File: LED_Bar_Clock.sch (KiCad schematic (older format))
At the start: 51 parts, among them J1 U262-16XN-4BVC11, J2 AVR-ISP-6, SW1 SKHMQKE010, SW2 SW_5_Way, U1 ATtiny84A-SSUR, U2 DS1307Z+, Y1 32.768 kHz

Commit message: Finish pcb routing
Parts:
- removed C2: 104, Capacitor_SMD:C_0603_1608Metric_Pad1.05x0.95mm_HandSolder, symbol Device:C_Small
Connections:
- net D+: now reaches R2.2, U1.2 (XTAL1/PB0)
- net D-: now reaches R3.2, U1.3 (XTAL2/PB1)
- net at U2.1 (X1): now also Y1.1; no longer Y1.2
- net at U2.2 (X2): now also Y1.2; no longer Y1.1
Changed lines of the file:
@@
 NoConn ~ 1700 6450
-$Comp
-L power:+5V #PWR0155
-U 1 1 5CA24AC6
-P 2300 5550
-F 0 "#PWR0155" H 2300 5400 50  0001 C CNN
-F 1 "+5V" H 2315 5723 50  0000 C CNN
-F 2 "" H 2300 5550 50  0001 C CNN
-F 3 "" H 2300 5550 50  0001 C CNN
-	1    2300 5550
-	-1   0    0    -1
-$EndComp
 $Comp
 L power:GND #PWR0157
@@
 U 1 1 5C8C5C64
 P 3150 6750
-F 0 "Y1" V 3196 6619 50  0000 R CNN
-F 1 "32.768 kHz" V 3105 6619 50  0000 R CNN
+F 0 "Y1" V 3104 6881 50  0000 L CNN
+F 1 "32.768 kHz" V 3195 6881 50  0000 L CNN
 F 2 "Crystal:Crystal_DS26_D2.0mm_L6.0mm_Horizontal" H 3150 6750 50  0001 C CNN
 F 3 "~" H 3150 6750 50  0001 C CNN
 	1    3150 6750
-	0    -1   -1   0
+	0    1    1    0
 $EndComp
 Wire Wire Line
@@
 $EndComp
 $Comp
-L Device:C_Small C2
-U 1 1 5CA3337C
-P 2450 5800
-F 0 "C2" H 2542 5846 50  0000 L CNN
-F 1 "104" H 2542 5755 50  0000 L CNN
-F 2 "Capacitor_SMD:C_0603_1608Metric_Pad1.05x0.95mm_HandSolder" H 2450 5800 50  0001 C CNN
-F 3 "~" H 2450 5800 50  0001 C CNN
-	1    2450 5800
-	1    0    0    -1
-$EndComp
-Wire Wire Line
-	2300 5550 2300 5650
-Wire Wire Line
-	2300 5650 2450 5650
-Wire Wire Line
-	2450 5650 2450 5700
-Connection ~ 2300 5650
-$Comp
-L power:GND #PWR0122
-U 1 1 5CA48238
-P 2450 5900
-F 0 "#PWR0122" H 2450 5650 50  0001 C CNN
-F 1 "GND" H 2455 5727 50  0000 C CNN
-F 2 "" H 2450 5900 50  0001 C CNN
-F 3 "" H 2450 5900 50  0001 C CNN
-	1    2450 5900
-	1    0    0    -1
-$EndComp
-Wire Wire Line
-	2300 5650 2300 6050
-$Comp
 L power:+5V #PWR0123
 U 1 1 5CA72611
@@
 	0    1    1    0
 $EndComp
+Text Label 2700 4250 0    50   ~ 0
+D+
+Text Label 2700 4350 0    50   ~ 0
+D-
+$Comp
+L power:+5V #PWR0155
+U 1 1 5CA24AC6
+P 2300 6050
+F 0 "#PWR0155" H 2300 5900 50  0001 C CNN
+F 1 "+5V" H 2315 6223 50  0000 C CNN
+F 2 "" H 2300 6050 50  0001 C CNN
+F 3 "" H 2300 6050 50  0001 C CNN
+	1    2300 6050
+	-1   0    0    -1
+$EndComp
 $EndSCHEMATC

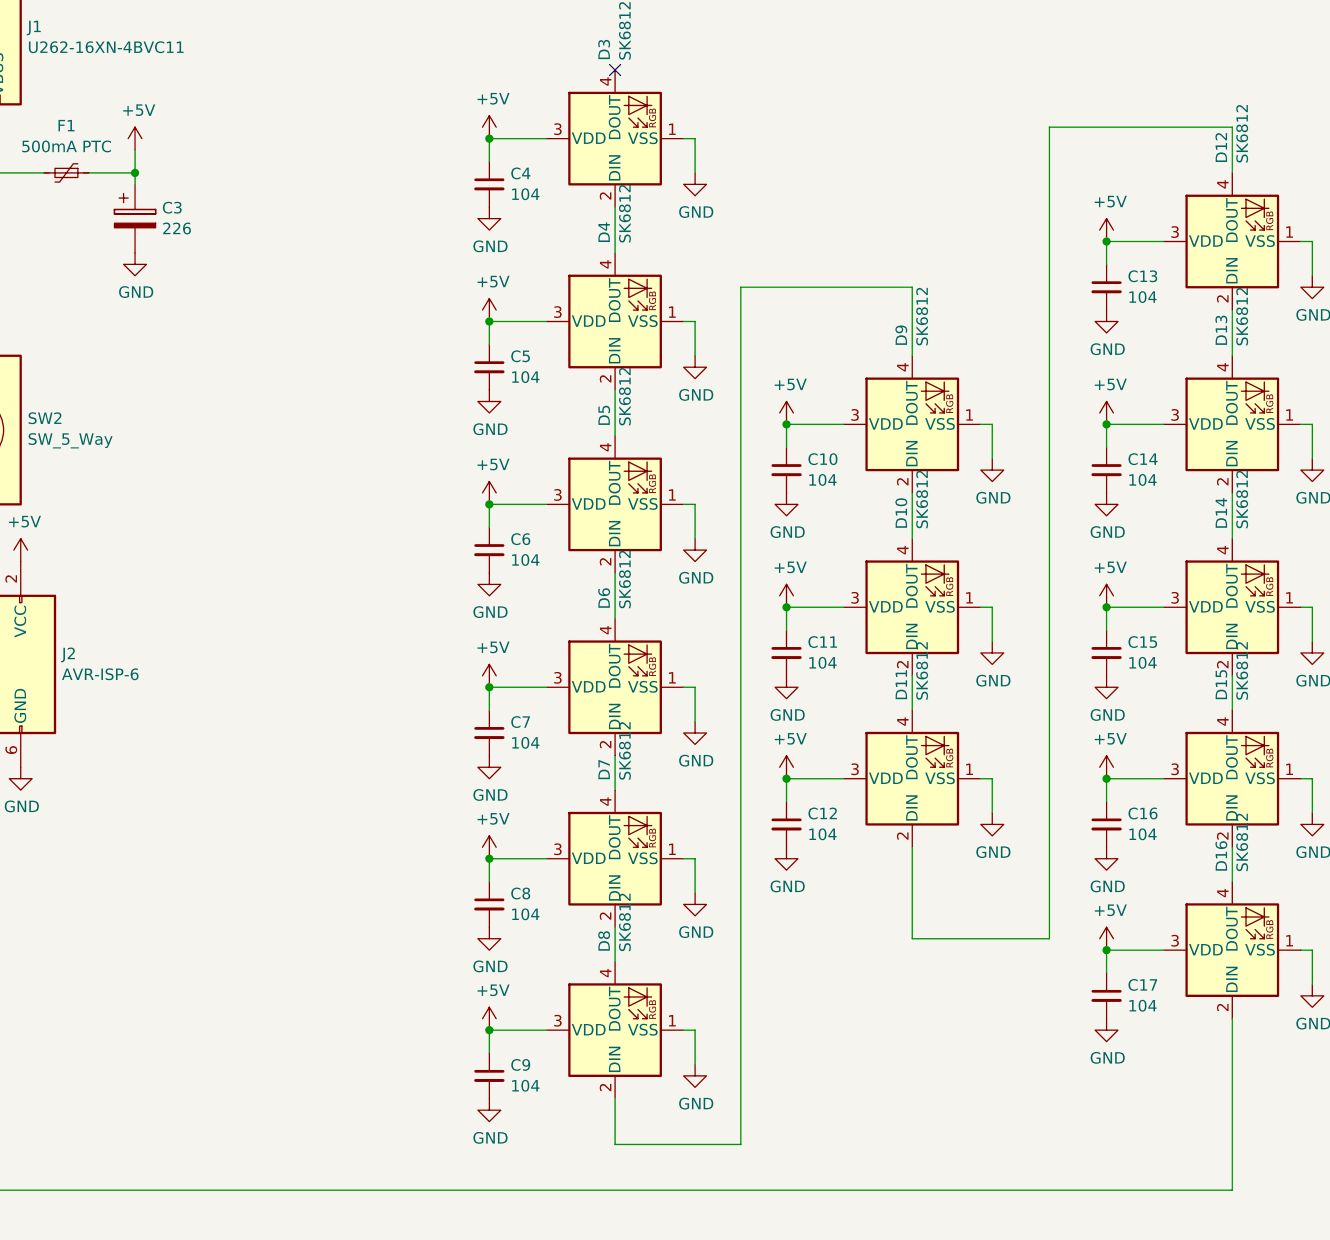
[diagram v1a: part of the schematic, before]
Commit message: fix annotations and silkscreen locations
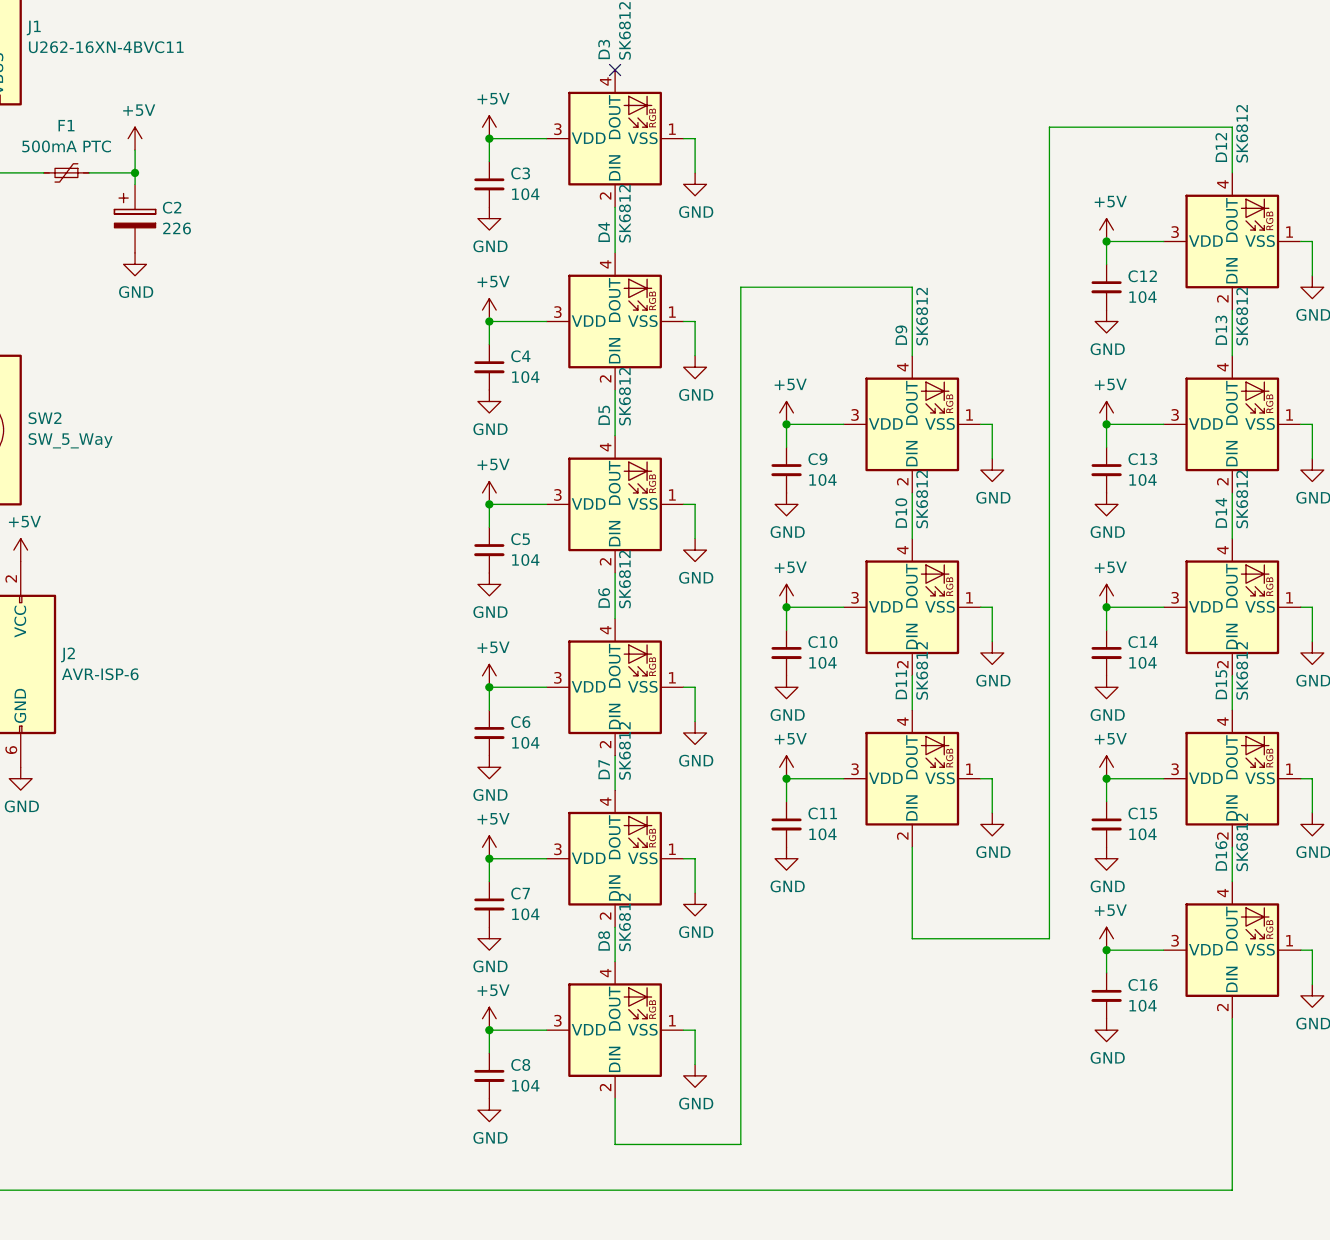
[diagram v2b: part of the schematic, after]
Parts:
- renumbered C11 to C10, C12 to C11, C13 to C12, C14 to C13, C15 to C14, C16 to C15, C17 to C16, C3 to C2, C4 to C3, C5 to C4, C6 to C5, C7 to C6, C8 to C7, C9 to C8, C10 to C9

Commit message: silkscreen and stealth labels
add a stealth footprint for the leds because we dont need silkscreen
on the front

official name is FILO Clock
first illuminated last out
.. or ..
first ignited last out
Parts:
- D10, D11, D12, D13, D14, D15, D16, D3, D4, D5, D6, D7, D8, D9: footprint LED_SMD:LED_SK6812_PLCC4_5.0x5.0mm_P3.2mm -> Clock_Footprints:LED_SK6812_PLCC4_5.0x5.0mm_P3.2mm_STEALTH
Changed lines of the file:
@@
 F 0 "D8" H 7541 5646 50  0000 L CNN
 F 1 "SK6812" H 7541 5555 50  0000 L CNN
-F 2 "LED_SMD:LED_SK6812_PLCC4_5.0x5.0mm_P3.2mm" H 7250 5300 50  0001 L TNN
+F 2 "Clock_Footprints:LED_SK6812_PLCC4_5.0x5.0mm_P3.2mm_STEALTH" H 7250 5300 50  0001 L TNN
 F 3 "https://cdn-shop.adafruit.com/product-files/1138/SK6812+LED+datasheet+.pdf" H 7300 5225 50  0001 L TNN
 	1    7200 5600
@@
 F 0 "D7" H 7541 4896 50  0000 L CNN
 F 1 "SK6812" H 7541 4805 50  0000 L CNN
-F 2 "LED_SMD:LED_SK6812_PLCC4_5.0x5.0mm_P3.2mm" H 7250 4550 50  0001 L TNN
+F 2 "Clock_Footprints:LED_SK6812_PLCC4_5.0x5.0mm_P3.2mm_STEALTH" H 7250 4550 50  0001 L TNN
 F 3 "https://cdn-shop.adafruit.com/product-files/1138/SK6812+LED+datasheet+.pdf" H 7300 4475 50  0001 L TNN
 	1    7200 4850
@@
 F 0 "D6" H 7541 4146 50  0000 L CNN
 F 1 "SK6812" H 7541 4055 50  0000 L CNN
-F 2 "LED_SMD:LED_SK6812_PLCC4_5.0x5.0mm_P3.2mm" H 7250 3800 50  0001 L TNN
+F 2 "Clock_Footprints:LED_SK6812_PLCC4_5.0x5.0mm_P3.2mm_STEALTH" H 7250 3800 50  0001 L TNN
 F 3 "https://cdn-shop.adafruit.com/product-files/1138/SK6812+LED+datasheet+.pdf" H 7300 3725 50  0001 L TNN
 	1    7200 4100
@@
 F 0 "D5" H 7541 3346 50  0000 L CNN
 F 1 "SK6812" H 7541 3255 50  0000 L CNN
-F 2 "LED_SMD:LED_SK6812_PLCC4_5.0x5.0mm_P3.2mm" H 7250 3000 50  0001 L TNN
+F 2 "Clock_Footprints:LED_SK6812_PLCC4_5.0x5.0mm_P3.2mm_STEALTH" H 7250 3000 50  0001 L TNN
 F 3 "https://cdn-shop.adafruit.com/product-files/1138/SK6812+LED+datasheet+.pdf" H 7300 2925 50  0001 L TNN
 	1    7200 3300
@@
 F 0 "D4" H 7541 2546 50  0000 L CNN
 F 1 "SK6812" H 7541 2455 50  0000 L CNN
-F 2 "LED_SMD:LED_SK6812_PLCC4_5.0x5.0mm_P3.2mm" H 7250 2200 50  0001 L TNN
+F 2 "Clock_Footprints:LED_SK6812_PLCC4_5.0x5.0mm_P3.2mm_STEALTH" H 7250 2200 50  0001 L TNN
 F 3 "https://cdn-shop.adafruit.com/product-files/1138/SK6812+LED+datasheet+.pdf" H 7300 2125 50  0001 L TNN
 	1    7200 2500
@@
 F 0 "D3" H 7541 1746 50  0000 L CNN
 F 1 "SK6812" H 7541 1655 50  0000 L CNN
-F 2 "LED_SMD:LED_SK6812_PLCC4_5.0x5.0mm_P3.2mm" H 7250 1400 50  0001 L TNN
+F 2 "Clock_Footprints:LED_SK6812_PLCC4_5.0x5.0mm_P3.2mm_STEALTH" H 7250 1400 50  0001 L TNN
 F 3 "https://cdn-shop.adafruit.com/product-files/1138/SK6812+LED+datasheet+.pdf" H 7300 1325 50  0001 L TNN
 	1    7200 1700
@@
 F 0 "D16" H 10241 5296 50  0000 L CNN
 F 1 "SK6812" H 10241 5205 50  0000 L CNN
-F 2 "LED_SMD:LED_SK6812_PLCC4_5.0x5.0mm_P3.2mm" H 9950 4950 50  0001 L TNN
+F 2 "Clock_Footprints:LED_SK6812_PLCC4_5.0x5.0mm_P3.2mm_STEALTH" H 9950 4950 50  0001 L TNN
 F 3 "https://cdn-shop.adafruit.com/product-files/1138/SK6812+LED+datasheet+.pdf" H 10000 4875 50  0001 L TNN
 	1    9900 5250
@@
 F 0 "D15" H 10241 4546 50  0000 L CNN
 F 1 "SK6812" H 10241 4455 50  0000 L CNN
-F 2 "LED_SMD:LED_SK6812_PLCC4_5.0x5.0mm_P3.2mm" H 9950 4200 50  0001 L TNN
+F 2 "Clock_Footprints:LED_SK6812_PLCC4_5.0x5.0mm_P3.2mm_STEALTH" H 9950 4200 50  0001 L TNN
 F 3 "https://cdn-shop.adafruit.com/product-files/1138/SK6812+LED+datasheet+.pdf" H 10000 4125 50  0001 L TNN
 	1    9900 4500
@@
 F 0 "D14" H 10241 3796 50  0000 L CNN
 F 1 "SK6812" H 10241 3705 50  0000 L CNN
-F 2 "LED_SMD:LED_SK6812_PLCC4_5.0x5.0mm_P3.2mm" H 9950 3450 50  0001 L TNN
+F 2 "Clock_Footprints:LED_SK6812_PLCC4_5.0x5.0mm_P3.2mm_STEALTH" H 9950 3450 50  0001 L TNN
 F 3 "https://cdn-shop.adafruit.com/product-files/1138/SK6812+LED+datasheet+.pdf" H 10000 3375 50  0001 L TNN
 	1    9900 3750
@@
 F 0 "D13" H 10241 2996 50  0000 L CNN
 F 1 "SK6812" H 10241 2905 50  0000 L CNN
-F 2 "LED_SMD:LED_SK6812_PLCC4_5.0x5.0mm_P3.2mm" H 9950 2650 50  0001 L TNN
+F 2 "Clock_Footprints:LED_SK6812_PLCC4_5.0x5.0mm_P3.2mm_STEALTH" H 9950 2650 50  0001 L TNN
 F 3 "https://cdn-shop.adafruit.com/product-files/1138/SK6812+LED+datasheet+.pdf" H 10000 2575 50  0001 L TNN
 	1    9900 2950
@@
 F 0 "D12" H 10241 2196 50  0000 L CNN
 F 1 "SK6812" H 10241 2105 50  0000 L CNN
-F 2 "LED_SMD:LED_SK6812_PLCC4_5.0x5.0mm_P3.2mm" H 9950 1850 50  0001 L TNN
+F 2 "Clock_Footprints:LED_SK6812_PLCC4_5.0x5.0mm_P3.2mm_STEALTH" H 9950 1850 50  0001 L TNN
 F 3 "https://cdn-shop.adafruit.com/product-files/1138/SK6812+LED+datasheet+.pdf" H 10000 1775 50  0001 L TNN
 	1    9900 2150
@@
 F 0 "D9" H 8841 2996 50  0000 L CNN
 F 1 "SK6812" H 8841 2905 50  0000 L CNN
-F 2 "LED_SMD:LED_SK6812_PLCC4_5.0x5.0mm_P3.2mm" H 8550 2650 50  0001 L TNN
+F 2 "Clock_Footprints:LED_SK6812_PLCC4_5.0x5.0mm_P3.2mm_STEALTH" H 8550 2650 50  0001 L TNN
 F 3 "https://cdn-shop.adafruit.com/product-files/1138/SK6812+LED+datasheet+.pdf" H 8600 2575 50  0001 L TNN
 	1    8500 2950
@@
 F 0 "D10" H 8841 3796 50  0000 L CNN
 F 1 "SK6812" H 8841 3705 50  0000 L CNN
-F 2 "LED_SMD:LED_SK6812_PLCC4_5.0x5.0mm_P3.2mm" H 8550 3450 50  0001 L TNN
+F 2 "Clock_Footprints:LED_SK6812_PLCC4_5.0x5.0mm_P3.2mm_STEALTH" H 8550 3450 50  0001 L TNN
 F 3 "https://cdn-shop.adafruit.com/product-files/1138/SK6812+LED+datasheet+.pdf" H 8600 3375 50  0001 L TNN
 	1    8500 3750
@@
 F 0 "D11" H 8841 4546 50  0000 L CNN
 F 1 "SK6812" H 8841 4455 50  0000 L CNN
-F 2 "LED_SMD:LED_SK6812_PLCC4_5.0x5.0mm_P3.2mm" H 8550 4200 50  0001 L TNN
+F 2 "Clock_Footprints:LED_SK6812_PLCC4_5.0x5.0mm_P3.2mm_STEALTH" H 8550 4200 50  0001 L TNN
 F 3 "https://cdn-shop.adafruit.com/product-files/1138/SK6812+LED+datasheet+.pdf" H 8600 4125 50  0001 L TNN
 	1    8500 4500
